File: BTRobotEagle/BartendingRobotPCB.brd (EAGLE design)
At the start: 154.9 x 100 mm, 32 parts, among them P1 B2B-XH-A(LF)(SN), P10 B2B-XH-A(LF)(SN), P11 B2B-XH-A(LF)(SN), P2 B2B-XH-A(LF)(SN), P3 B2B-XH-A(LF)(SN), P4 B2B-XH-A(LF)(SN), P5 B2B-XH-A(LF)(SN), P6 B2B-XH-A(LF)(SN), P7 B2B-XH-A(LF)(SN), P8 B2B-XH-A(LF)(SN), P9 B2B-XH-A(LF)(SN), U10 MCP23017-E/SP, U11 MCP23017-E/SP

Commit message: BRD/SCH upgrades
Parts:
- removed 12VMOTORS: L298N, BartendingRobot:L298N
- removed SHAKESTEPCON, SLIDESTEPCON: B4B-XH-A(LF)(SN), BartendingRobot:JST_B4B-XH-A(LF)(SN)
- removed U10, U11: MCP23017-E/SP, BartendingRobot:DIP787W45P254L3556H508Q28
- added 1K: 10MMCAP, BartendingRobot:10MMCAP
- added L1: L298N, BartendingRobot:L298N
- added MCP1, MCP2: MCP23017-E/SP, BartendingRobot:DIP787W45P254L3556H508Q28
- added SP1: 2PORTSCREW, BartendingRobot:2PORTSCREW
- added STEPSHAKE, STEPSLIDE: B4B-XH-A(LF)(SN), BartendingRobot:JST_B4B-XH-A(LF)(SN)
- moved SLIDESTOP 145.7 mm to (128.3, 94.2)
- moved P11 144.0 mm to (95.2, 94.2), turned to 0 degrees
- moved P10 131.5 mm to (86.4, 94.2), turned to 0 degrees
- moved SHAKESTOP 123.3 mm to (116.8, 94.2)
- moved P9 119.0 mm to (77.5, 94.2), turned to 0 degrees
- moved P8 106.6 mm to (68.6, 94.2), turned to 0 degrees
- moved BARSTOP 104.3 mm to (105.4, 94.2)
- moved PC6 100.2 mm to (99.1, 80.3), turned to 0 degrees
- moved PC5 97.2 mm to (82.5, 80.3), turned to 0 degrees
- moved P7 94.2 mm to (59.7, 94.2), turned to 0 degrees
- moved PC4 93.2 mm to (64.8, 80.3), turned to 0 degrees
- moved P6 81.9 mm to (50.8, 94.2), turned to 0 degrees
- moved P5 69.6 mm to (41.9, 94.2), turned to 0 degrees
- moved PC3 66.0 mm to (47.0, 80.3), turned to 0 degrees
- moved P4 57.5 mm to (33.0, 94.2), turned to 0 degrees
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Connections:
- removed net N$31: P9.2, PC5.6
- removed net N$32: P9.1, PC5.3
- removed net N$35: P7.2, PC4.6
- removed net N$36: P7.1, PC4.3
- removed net SHIELD: PI.S1, PI.S2, PI.S3, PI.S4
- new net N$10: P3.2, PC2.3
- new net N$20: P11.2, PC6.3
- new net N$25: P1.1, PC1.6
- new net N$9: P3.1, PC2.6
- net 0: now also MCP1.1; no longer U11.21
- net 1: now also MCP1.2; no longer U11.22
- net 10: now also MCP1.22; no longer U11.3
- net 11: now also MCP1.5; no longer U11.4
- net 12: now also MCP1.6; no longer U11.5
- net 12V: now also 1K.+, L1.12V, SP1.P1
- net 13: now also MCP1.7; no longer U11.6
- net 14: now also MCP1.8; no longer U11.7
- net 15: now also MCP2.3; no longer U10.21
- net 16: now also MCP2.2; no longer U10.22
- net 17: now also MCP2.1; no longer U10.23
- net 18: now also MCP2.28; no longer U10.24
- net 19: now also MCP2.27; no longer U10.25
- net 2: now also MCP1.3; no longer U11.23
- net 20: now also MCP2.26; no longer U10.26
- net 21: now also MCP2.23; no longer U10.27
- net 22: now also MCP2.24; no longer U10.28
- net 23: now also MCP2.25; no longer U10.1
- net 24: now also MCP2.4; no longer U10.2
- net 25: now also MCP2.22; no longer U10.3
- net 26: now also MCP2.21; no longer U10.4
- net 27: now also MCP2.8; no longer U10.5
- net 28: now also MCP2.7; no longer U10.6
- net 29: now also MCP2.6; no longer U10.7
- net 3: now also MCP1.26; no longer U11.24
- net 3.3V: now also MCP1.18, MCP1.9, MCP2.15, MCP2.18, MCP2.9; no longer BARSTOP.1, SHAKESTOP.1, SLIDESTOP.1, U10.15, U10.18, U10.9, U11.18, U11.9
- net 4: now also MCP1.27; no longer U11.25
- net 5: now also MCP1.28; no longer U11.26
- net 5V: now also BARSTOP.1, SHAKESTOP.1, SLIDESTOP.1
- net 6: now also MCP1.25; no longer U11.27
- net 7: now also MCP1.24; no longer U11.28
- net 8: now also MCP1.23; no longer U11.1
- net 9: now also MCP1.21; no longer U11.2
- net BARST: now also PI.19; no longer PI.21
- net CGND: now also 1K.-, L1.GND, MCP1.10, MCP1.15, MCP1.16, MCP1.17, MCP2.10, MCP2.16, MCP2.17, PI.S1, PI.S2, PI.S3, PI.S4, SP1.P2; no longer U10.10, U10.16, U10.17, U11.10, U11.15, U11.16, U11.17
- net ICE1: now also L1.IN4; no longer 12VMOTORS.IN1
- net ICE2: now also L1.IN3; no longer 12VMOTORS.IN2
- net ICEEN: now also L1.ENB; no longer 12VMOTORS.ENA
- net N$1: now also SHAKESTEP.14, STEPSHAKE.1; no longer SHAKESTEP.12, SHAKESTEPCON.4
- net N$11: now also P7.1, PC4.6; no longer P1.1, PC1.3
- net N$12: now also P7.2, PC4.3; no longer P1.2, PC1.6
- net N$15: now also P9.1, PC5.6; no longer P3.1, PC2.3
- net N$16: now also P9.2, PC5.3; no longer P3.2, PC2.6
- net N$19: now also P11.1, PC6.6; no longer P5.1, PC3.3
- net N$2: now also SHAKESTEP.13, STEPSHAKE.2; no longer SHAKESTEP.11, SHAKESTEPCON.3
- net N$21: now also P5.1; no longer P5.2
- net N$24: now also P5.2, PC3.3; no longer P11.1, PC6.3
- net N$26: now also P1.2, PC1.3; no longer P11.2, PC6.6
- net N$3: now also SHAKESTEP.11, STEPSHAKE.4; no longer SHAKESTEP.13, SHAKESTEPCON.2
- net N$4: now also SHAKESTEP.12, STEPSHAKE.3; no longer SHAKESTEP.14, SHAKESTEPCON.1
- net N$5: now also SLIDESTEP.14, STEPSLIDE.1; no longer SLIDESTEP.12, SLIDESTEPCON.4
- net N$6: now also SLIDESTEP.13, STEPSLIDE.2; no longer SLIDESTEP.11, SLIDESTEPCON.3
- net N$7: now also SLIDESTEP.11, STEPSLIDE.4; no longer SLIDESTEP.13, SLIDESTEPCON.2
- net N$8: now also SLIDESTEP.12, STEPSLIDE.3; no longer SLIDESTEP.14, SLIDESTEPCON.1
- net SCL: now also MCP1.12, MCP2.12; no longer U10.12, U11.12
- net SDA: now also MCP1.13, MCP2.13; no longer U10.13, U11.13
- net SHAKE1: now also L1.IN1; no longer 12VMOTORS.IN3
- net SHAKE2: now also L1.IN2; no longer 12VMOTORS.IN4
- net SHAKEEN: now also L1.ENA; no longer 12VMOTORS.ENB
- net SHAKEST: now also PI.21; no longer PI.19
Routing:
- net 5V: track 218.8 -> 0.00 mm, vias 2 -> 0
- net SLIDEDIR: track 0.00 -> 175.9 mm
- net SLIDESTEP: track 0.00 -> 171.4 mm
- net SLIDESLP: track 0.00 -> 167.7 mm
- net ICEEN: track 0.00 -> 167.6 mm
- net SHAKEEN: track 0.00 -> 154.8 mm
- net SHAKE1: track 0.00 -> 153.7 mm
- net SHAKE2: track 0.00 -> 152.6 mm
- net ICE2: track 0.00 -> 151.4 mm
- net ICE1: track 0.00 -> 150.2 mm
- net SHAKEDIR: track 0.00 -> 132.9 mm
- net SHAKESTEP: track 0.00 -> 131.0 mm
- net SLIDEST: track 0.00 -> 127.0 mm
- net SHAKEST: track 0.00 -> 118.9 mm
- net SHAKESLP: track 0.00 -> 117.0 mm
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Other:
- board size 154.9 x 100 mm -> 162.6 x 100.3 mm
- board text added: "C:/Temp/PEI Logo.bmp"

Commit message: update brd/sch
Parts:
- added C3, C4: 10MMCAP, BartendingRobot:10MMCAP
- added MGT1, MGT2, MGT3, MGT4, MGT5, MGT6, MGT7, MGT8: MOUNTING_HOLE, BartendingRobot:MOUNTING_HOLE
- moved 1K 6.86 mm to (131.6, 6.32)
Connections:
- net 12V: now also C3.+, C4.+
- net CGND: now also C3.-, C4.-, MGT1.P$1, MGT2.P$1, MGT3.P$1, MGT4.P$1, MGT5.P$1, MGT6.P$1, MGT7.P$1, MGT8.P$1
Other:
- board text removed: "C:/Temp/PEI Logo.bmp"

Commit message: more changes
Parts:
- added C5, C6, C7: SMALLCAP, BartendingRobot:SMALLCAP
- moved 1K 6.35 mm to (125.3, 6.32)
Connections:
- net 12V: now also C5.+; no longer C3.+, C4.+
- net 5V: now also C3.+, C7.+
- net 8.6V: now also C4.+, C6.+
- net CGND: now also C5.-, C6.-, C7.-
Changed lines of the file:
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@@
 <attribute name="VALUE" x="162.3822" y="58.4556" size="1.27" layer="27" font="vector" ratio="12" rot="R180"/>
 </element>
-<element name="1K" library="BartendingRobot" package="10MMCAP" value="10MMCAP" x="131.6482" y="6.3246" smashed="yes" rot="R270">
-<attribute name="NAME" x="137.6482" y="9.3246" size="1.778" layer="25" font="vector" rot="R270"/>
-<attribute name="VALUE" x="124.6482" y="9.3246" size="1.778" layer="27" font="vector" rot="R270"/>
+<element name="1K" library="BartendingRobot" package="10MMCAP" value="10MMCAP" x="125.2982" y="6.3246" smashed="yes" rot="R270">
+<attribute name="NAME" x="131.2982" y="9.3246" size="1.778" layer="25" font="vector" rot="R270"/>
+<attribute name="VALUE" x="118.2982" y="9.3246" size="1.778" layer="27" font="vector" rot="R270"/>
 </element>
 <element name="SP1" library="BartendingRobot" package="2PORTSCREW" value="2PORTSCREW" x="155.0162" y="3.9116" smashed="yes" rot="R180">
@@
 <element name="MGT7" library="BartendingRobot" package="MOUNTING_HOLE" value="MOUNTING_HOLE" x="111.76" y="85.09" smashed="yes"/>
 <element name="MGT8" library="BartendingRobot" package="MOUNTING_HOLE" value="MOUNTING_HOLE" x="121.92" y="76.2" smashed="yes"/>
+<element name="C5" library="BartendingRobot" package="SMALLCAP" value="SMALLCAP" x="137.16" y="5.842" smashed="yes" rot="R270">
+<attribute name="NAME" x="142.24" y="8.382" size="1.27" layer="25" font="vector" rot="R270"/>
+<attribute name="VALUE" x="130.81" y="8.382" size="1.27" layer="27" font="vector" rot="R270"/>
+</element>
+<element name="C6" library="BartendingRobot" package="SMALLCAP" value="SMALLCAP" x="106.172" y="43.942" smashed="yes">
+<attribute name="NAME" x="103.632" y="47.117" size="1.27" layer="25" font="vector"/>
+<attribute name="VALUE" x="103.632" y="39.497" size="1.27" layer="27" font="vector"/>
+</element>
+<element name="C7" library="BartendingRobot" package="SMALLCAP" value="SMALLCAP" x="74.93" y="43.688" smashed="yes">
+<attribute name="NAME" x="72.39" y="46.863" size="1.27" layer="25" font="vector"/>
+<attribute name="VALUE" x="72.39" y="39.243" size="1.27" layer="27" font="vector"/>
+</element>
 </elements>
 <signals>
@@
 <contactref element="PI" pad="S1"/>
 <contactref element="PI" pad="S2"/>
-<contactref element="C3" pad="-"/>
-<contactref element="C4" pad="-"/>
 <contactref element="MGT3" pad="P$1"/>
 <contactref element="MGT4" pad="P$1"/>
@@
 <contactref element="MGT7" pad="P$1"/>
 <contactref element="MGT8" pad="P$1"/>
+<contactref element="C5" pad="-"/>
+<contactref element="C3" pad="-"/>
+<contactref element="C4" pad="-"/>
+<contactref element="C7" pad="-"/>
+<contactref element="C6" pad="-"/>
 <wire x1="147.1422" y1="72.5856" x2="147.1422" y2="87.8256" width="0" layer="19" extent="1-1"/>
 <wire x1="152.2022" y1="61.1556" x2="147.1422" y2="72.5856" width="0" layer="19" extent="1-1"/>
@@
 <wire x1="90.7386" y1="54.6124" x2="81.28" y2="67.689" width="0" layer="19" extent="1-1"/>
 <wire x1="82.55" y1="43.815" x2="90.7386" y2="54.6124" width="0" layer="19" extent="1-1"/>
+<wire x1="76.2" y1="43.688" x2="82.55" y2="43.815" width="0" layer="19" extent="1-1"/>
 <wire x1="117.0784" y1="54.6632" x2="133.1522" y2="61.1556" width="0" layer="19" extent="1-1"/>
+<wire x1="107.442" y1="43.942" x2="117.0784" y2="54.6632" width="0" layer="19" extent="1-1"/>
 <wire x1="144.78" y1="43.815" x2="152.2022" y2="61.1556" width="0" layer="19" extent="1-1"/>
 <wire x1="158.7922" y1="27.8256" x2="144.78" y2="43.815" width="0" layer="19" extent="1-1"/>
 <wire x1="152.5162" y1="3.9116" x2="158.7922" y2="27.8256" width="0" layer="19" extent="1-1"/>
 <wire x1="144.78" y1="6.35" x2="152.5162" y2="3.9116" width="0" layer="19" extent="1-1"/>
-<wire x1="131.6482" y1="3.5746" x2="144.78" y2="6.35" width="0" layer="19" extent="1-1"/>
-<wire x1="117.0784" y1="4.1632" x2="131.6482" y2="3.5746" width="0" layer="19" extent="1-1"/>
+<wire x1="137.16" y1="4.572" x2="144.78" y2="6.35" width="0" layer="19" extent="1-1"/>
+<wire x1="125.2982" y1="3.5746" x2="137.16" y2="4.572" width="0" layer="19" extent="1-1"/>
+<wire x1="117.0784" y1="4.1632" x2="125.2982" y2="3.5746" width="0" layer="19" extent="1-1"/>
 <wire x1="90.7386" y1="4.1124" x2="117.0784" y2="4.1632" width="0" layer="19" extent="1-1"/>
 <wire x1="82.55" y1="6.35" x2="90.7386" y2="4.1124" width="0" layer="19" extent="1-1"/>
@@
 <contactref element="BARSTOP" pad="1"/>
 <contactref element="SHAKESTOP" pad="1"/>
+<contactref element="C3" pad="+"/>
+<contactref element="C7" pad="+"/>
 <wire x1="119.34" y1="94.234" x2="130.77" y2="94.234" width="0" layer="19" extent="1-1"/>
 <wire x1="107.91" y1="94.234" x2="119.34" y2="94.234" width="0" layer="19" extent="1-1"/>
 <wire x1="103.46" y1="89.154" x2="107.91" y2="94.234" width="0" layer="19" extent="1-1"/>
+<wire x1="121.92" y1="82.34" x2="119.34" y2="94.234" width="0" layer="19" extent="1-1"/>
 <wire x1="86.95" y1="89.154" x2="103.46" y2="89.154" width="0" layer="19" extent="1-1"/>
 <wire x1="69.17" y1="89.154" x2="86.95" y2="89.154" width="0" layer="19" extent="1-1"/>
@@
 <wire x1="15.83" y1="89.154" x2="33.61" y2="89.154" width="0" layer="19" extent="1-1"/>
 <wire x1="69.7386" y1="54.6124" x2="69.17" y2="89.154" width="0" layer="19" extent="1-1"/>
+<wire x1="73.66" y1="43.688" x2="69.7386" y2="54.6124" width="0" layer="19" extent="1-1"/>
 <wire x1="57.498" y1="54.472" x2="69.7386" y2="54.6124" width="0" layer="19" extent="1-1"/>
 <wire x1="54.958" y1="54.472" x2="57.498" y2="54.472" width="0" layer="19" extent="1-1"/>
@@
 <contactref element="PC2" pad="8"/>
 <contactref element="8.6V" pad="OUT+"/>
+<contactref element="C4" pad="+"/>
+<contactref element="C6" pad="+"/>
+<wire x1="94.66" y1="71.374" x2="111.76" y2="78.95" width="0" layer="19" extent="1-1"/>
 <wire x1="78.15" y1="71.374" x2="94.66" y2="71.374" width="0" layer="19" extent="1-1"/>
 <wire x1="96.0784" y1="54.6632" x2="94.66" y2="71.374" width="0" layer="19" extent="1-1"/>
+<wire x1="104.902" y1="43.942" x2="96.0784" y2="54.6632" width="0" layer="19" extent="1-1"/>
 <wire x1="60.37" y1="71.374" x2="78.15" y2="71.374" width="0" layer="19" extent="1-1"/>
 <wire x1="42.59" y1="71.374" x2="60.37" y2="71.374" width="0" layer="19" extent="1-1"/>
@@
 <contactref element="1K" pad="+"/>
 <contactref element="SP1" pad="P1"/>
-<contactref element="C3" pad="+"/>
-<contactref element="C4" pad="+"/>
+<contactref element="C5" pad="+"/>
 <wire x1="149.7022" y1="61.1556" x2="147.1422" y2="70.0456" width="0" layer="19" extent="1-1"/>
 <wire x1="129.3622" y1="70.0456" x2="147.1422" y2="70.0456" width="0" layer="19" extent="1-1"/>
 <wire x1="130.6522" y1="61.1556" x2="129.3622" y2="70.0456" width="0" layer="19" extent="1-1"/>
-<wire x1="121.92" y1="82.34" x2="129.3622" y2="70.0456" width="0" layer="19" extent="1-1"/>
-<wire x1="111.76" y1="78.95" x2="121.92" y2="82.34" width="0" layer="19" extent="1-1"/>
 <wire x1="158.7922" y1="22.8256" x2="149.7022" y2="61.1556" width="0" layer="19" extent="1-1"/>
 <wire x1="157.5162" y1="3.9116" x2="158.7922" y2="22.8256" width="0" layer="19" extent="1-1"/>
-<wire x1="131.6482" y1="9.0746" x2="157.5162" y2="3.9116" width="0" layer="19" extent="1-1"/>
-<wire x1="96.0784" y1="4.1632" x2="131.6482" y2="9.0746" width="0" layer="19" extent="1-1"/>
+<wire x1="137.16" y1="7.112" x2="157.5162" y2="3.9116" width="0" layer="19" extent="1-1"/>
+<wire x1="125.2982" y1="9.0746" x2="137.16" y2="7.112" width="0" layer="19" extent="1-1"/>
+<wire x1="96.0784" y1="4.1632" x2="125.2982" y2="9.0746" width="0" layer="19" extent="1-1"/>
 <wire x1="69.7386" y1="4.1124" x2="96.0784" y2="4.1632" width="0" layer="19" extent="1-1"/>
 </signal>

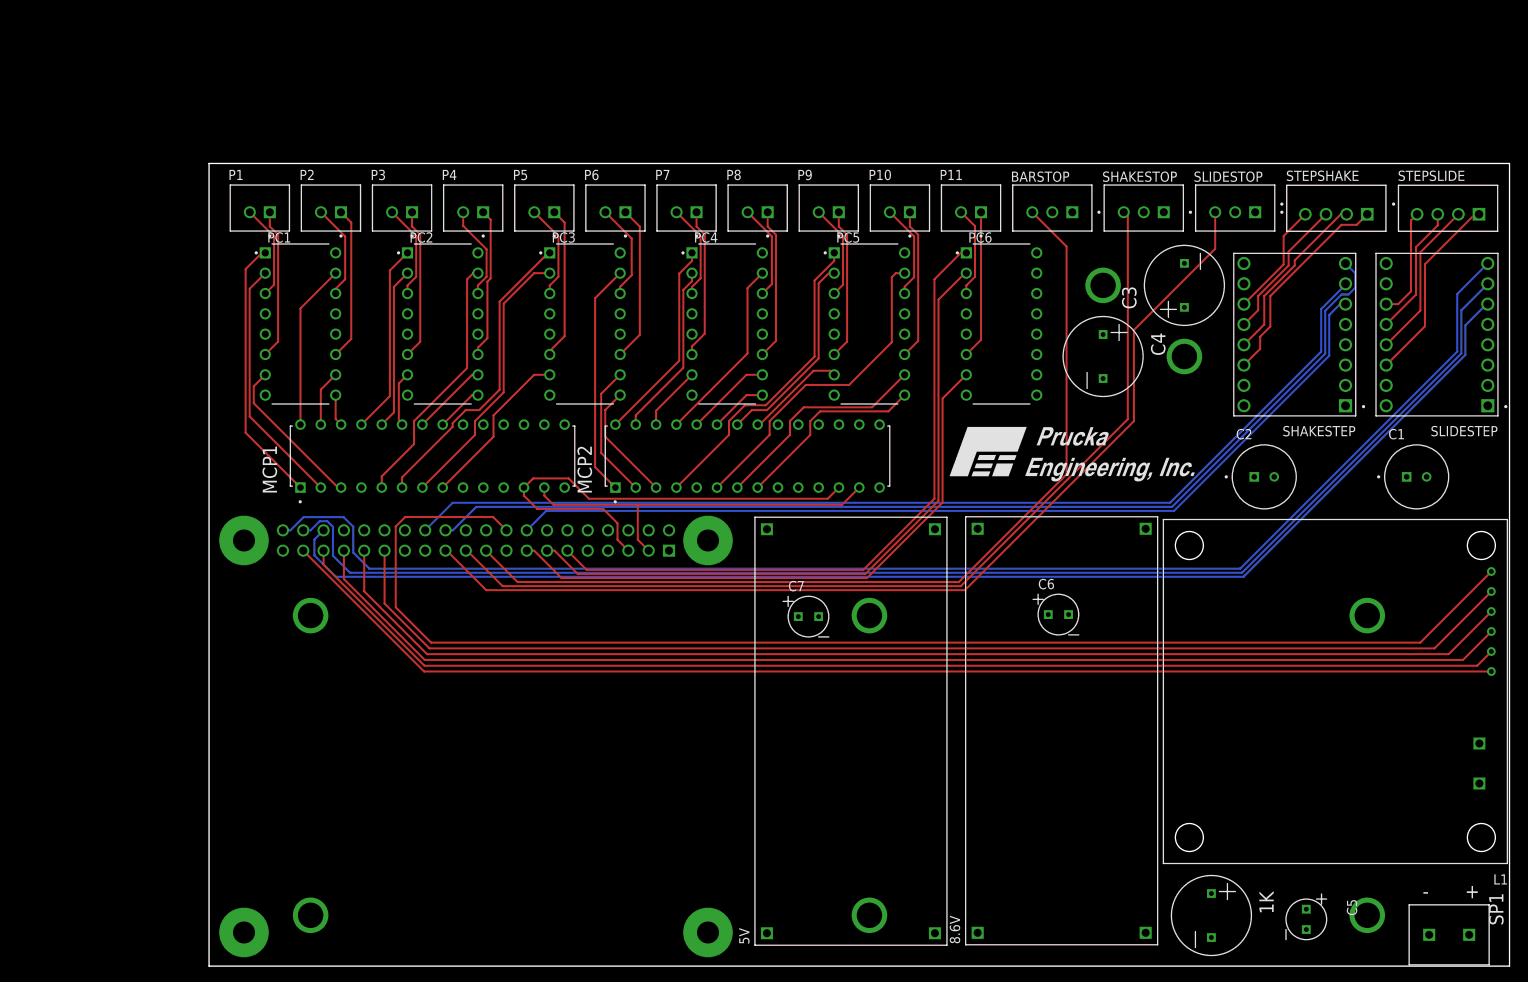
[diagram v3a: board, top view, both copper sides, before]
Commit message: finish power and ground traces
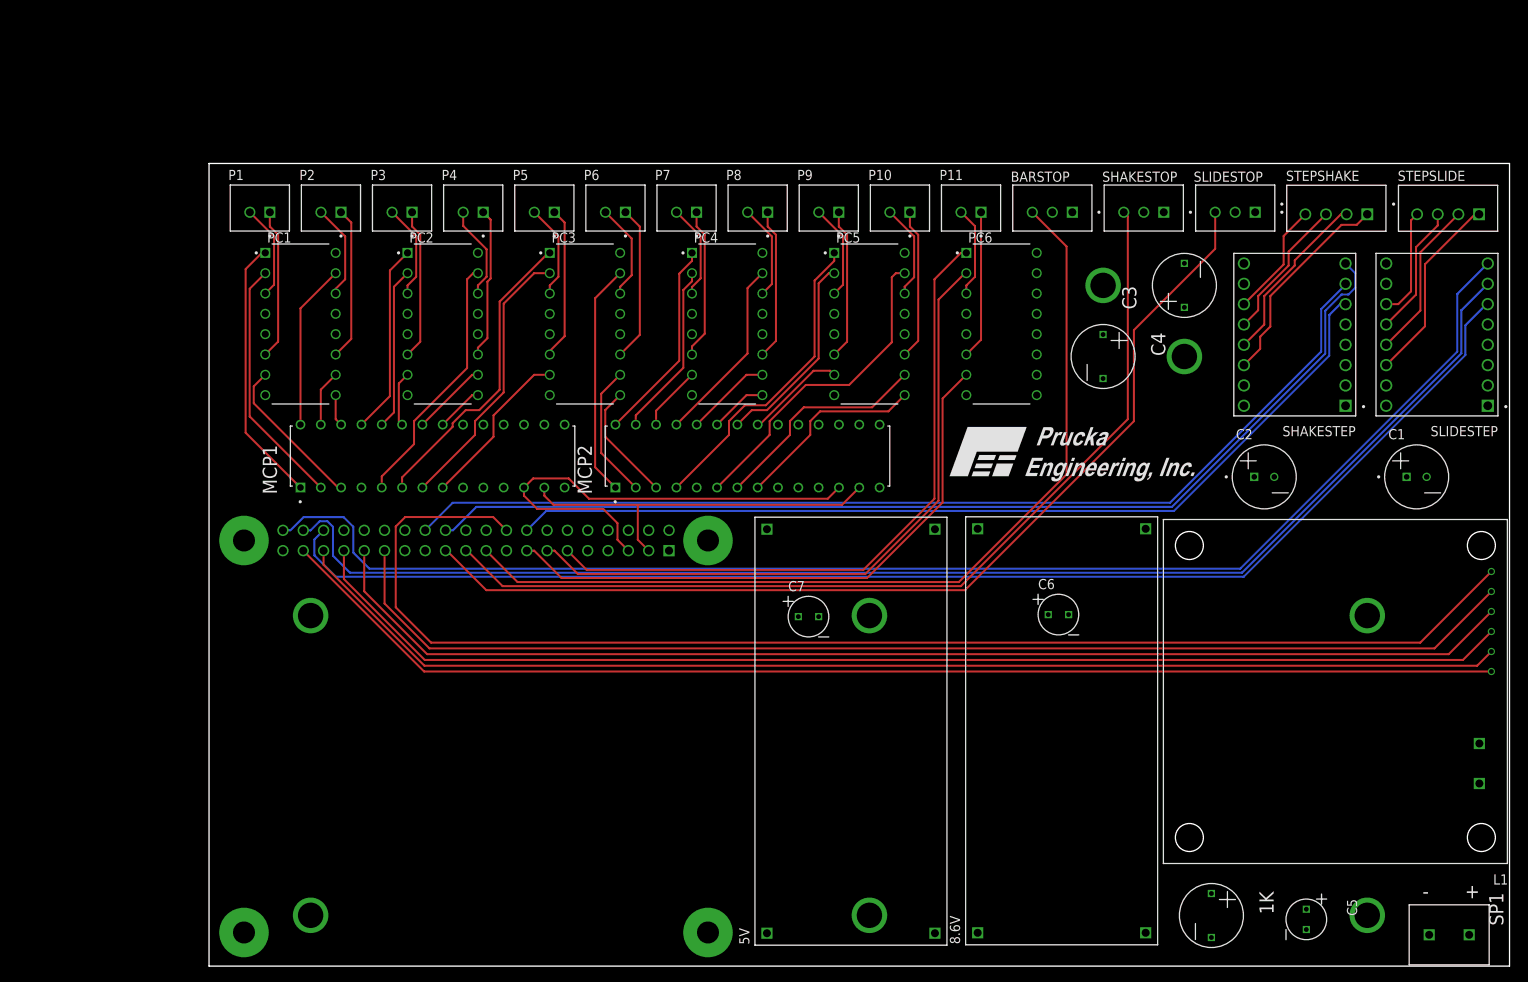
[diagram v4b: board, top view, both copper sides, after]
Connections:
- net 3.3V: now also BARSTOP.1, SHAKESTOP.1, SLIDESTOP.1
- net 5V: no longer BARSTOP.1, SHAKESTOP.1, SLIDESTOP.1
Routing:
- added copper zone on layer 15, net 12V
- added copper zone on layer 15, net 3.3V
- added copper zone on layer 15, net 5V
- added copper zone on layer 15, net 8.6V
- added copper zone on layer 2, net CGND
